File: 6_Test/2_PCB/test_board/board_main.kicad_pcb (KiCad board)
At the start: 4 copper layers, 105.5 x 83 mm, 81 parts, among them J1 PWR_Supply_Pins, J10 Chip_AVSS_GND_Jumpers, J11 Buffer_PWR_Jumper, J12 Reset_PWR_Jumpers, J13 Reset_Signal_Jumpers, J14 1546551-4, J2 Analog_Input_Pins, J3 Digital_Input_Pins, J4 Digital_Output_Pins, J5 Chip_VDD_Jumpers, J6 BNC_Odd, J7 BNC_Even, J8 BNC_Jumpers, J9 Analog_Input_Jumpers, U1 TPS74501PDRVR, U2 ADA4807-1AKSZ-R7, U3 ADA4807-1AKSZ-R7, U4 TPS74501PDRVR, U5 SN74HC74DR, U6 CD4001BM96, U7 SN74LVC245APWR, U8 SN74LVC245APWR

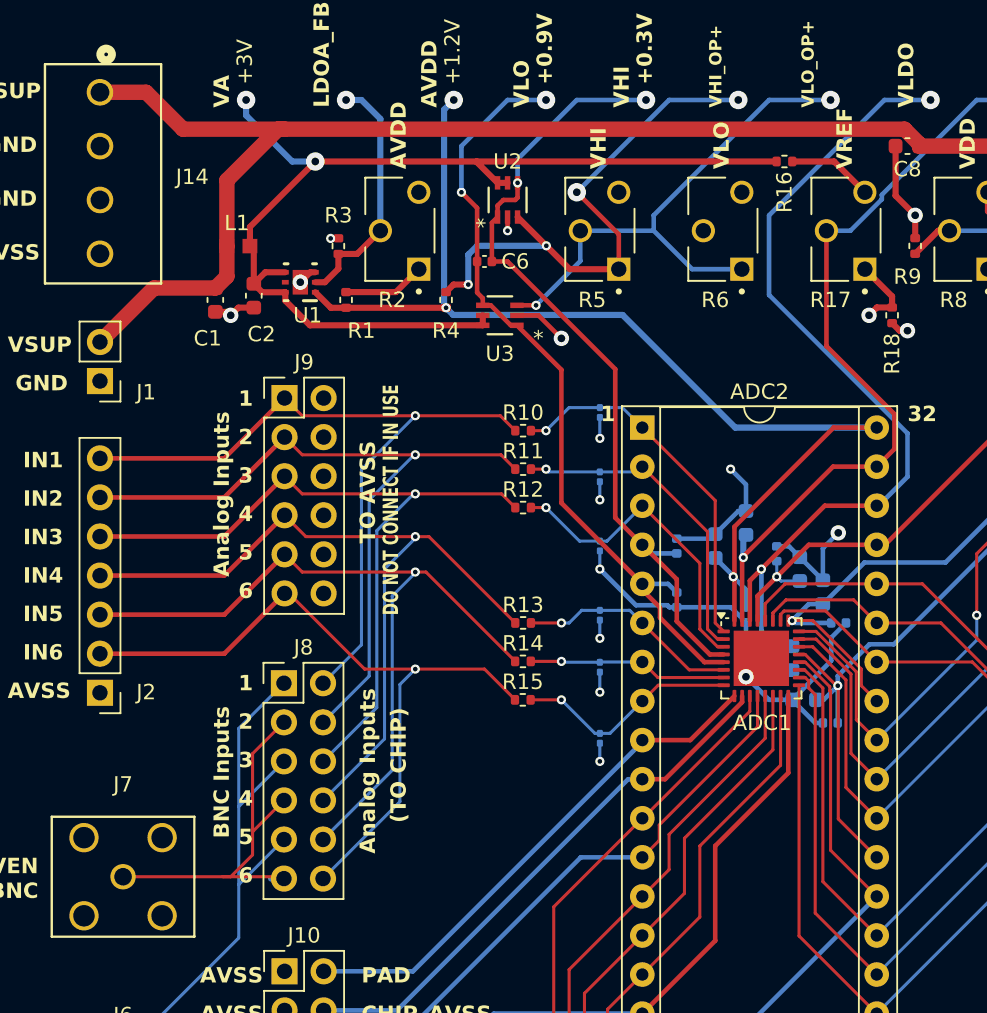
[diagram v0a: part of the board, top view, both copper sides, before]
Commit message: Adjusted potentiometers
Equally spaced potentiometers & added additional silkscreen
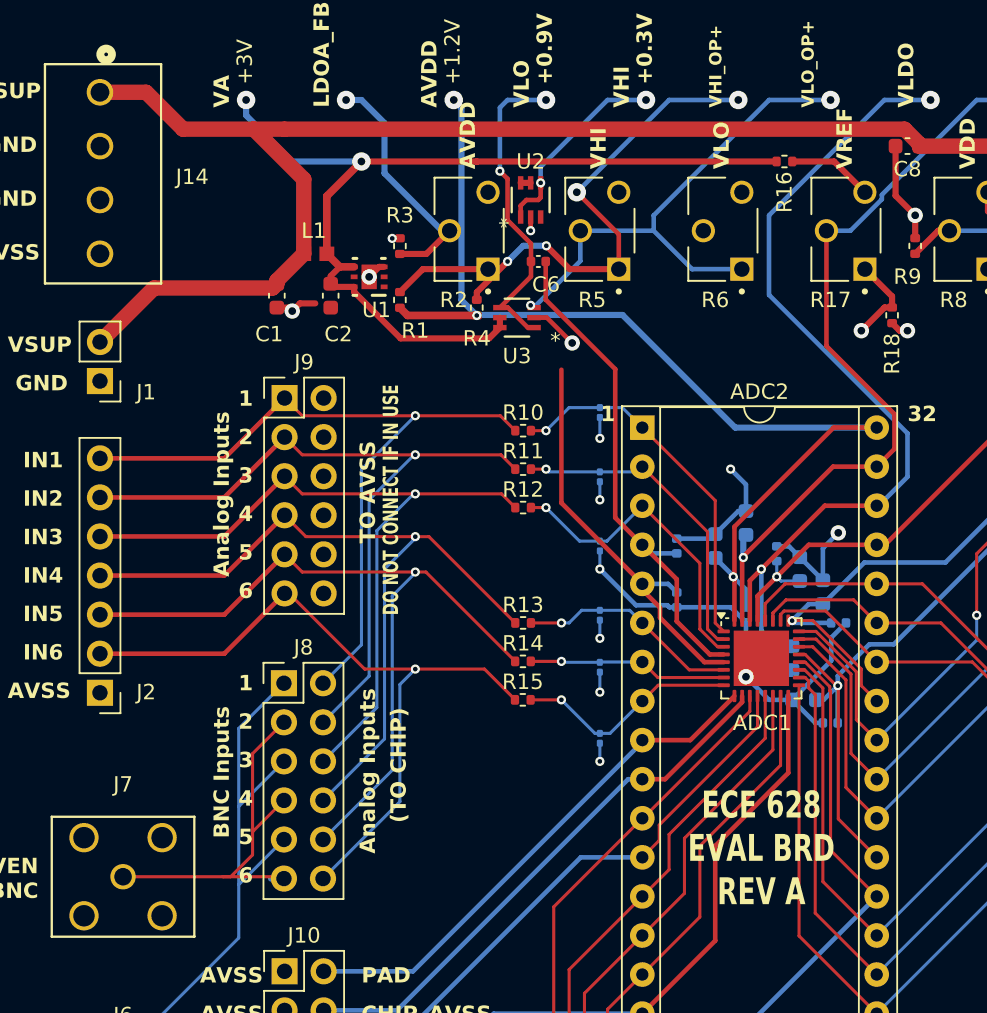
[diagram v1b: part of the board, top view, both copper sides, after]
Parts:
- moved L1 5.02 mm to (93.0, 76.0)
- moved C2 5.00 mm to (94.0, 78.7)
- moved R2 4.50 mm to (103.0, 74.5)
- moved U1 4.49 mm to (96.5, 77.5)
- moved C1 4.01 mm to (90.5, 78.7)
- moved R3 4.00 mm to (98.5, 75.5)
- moved C6 3.50 mm to (107.5, 76.5)
- moved R1 3.50 mm to (98.5, 79.0)
- moved R4 2.06 mm to (103.5, 79.5)
- moved U2 1.50 mm to (107.0, 72.5)
- moved U3 1.12 mm to (106.1, 80.1)
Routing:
- net /AnalogSupply/VA: track 68.5 -> 61.4 mm
- net /ADC/VHI: track 53.1 -> 46.2 mm
- net Net-(U2-+IN): track 36.0 -> 30.7 mm
- net /ADC/AVDD: track 76.0 -> 71.0 mm
- net /ADC/VLO: track 51.1 -> 47.2 mm
- net /AnalogSupply/VSUP: track 98.4 -> 102.2 mm
- net Net-(R1-Pad2): track 5.35 -> 6.35 mm
- net Net-(R17-Pad1): track 4.93 -> 5.85 mm
- net Net-(U3-+IN): track 34.4 -> 33.5 mm
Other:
- board text added: "DN"
- board text added: "ECE 628 EVAL BRD REV A"
- board text added: "UN"

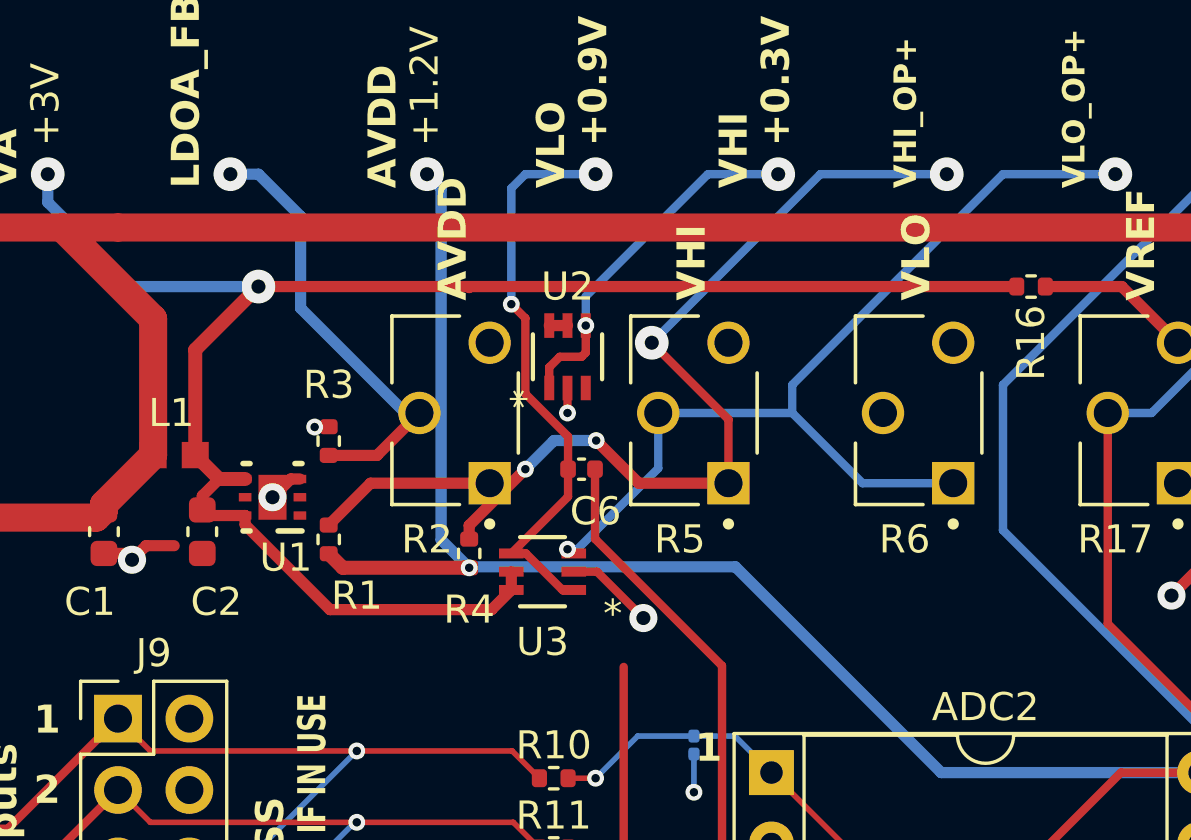
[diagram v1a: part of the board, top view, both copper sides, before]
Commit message: fixed overlapping net issues on final revision
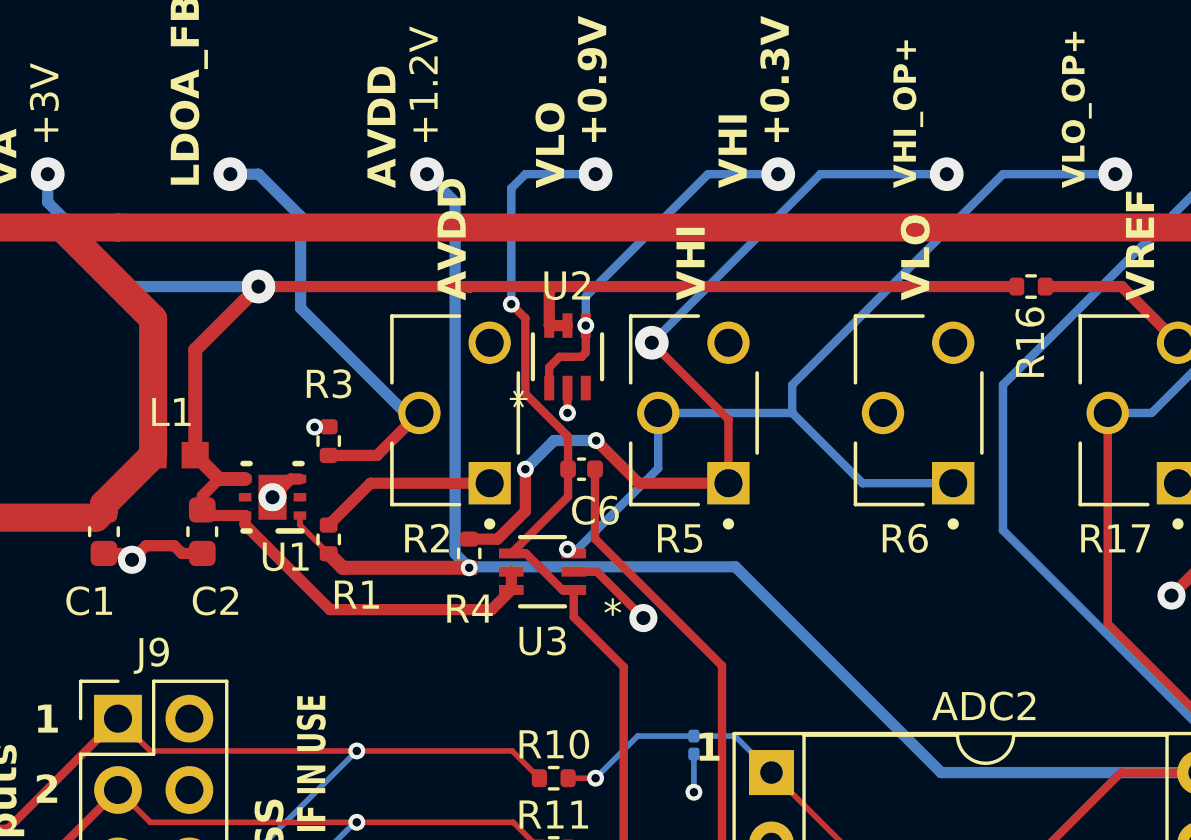
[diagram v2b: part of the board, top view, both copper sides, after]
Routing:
- net /ADC/VLO: track 47.2 -> 50.7 mm
- net /ADC/AVDD: track 71.0 -> 72.8 mm
- net /AnalogSupply/VA: track 61.4 -> 62.9 mm
- net GND: track 117.4 -> 118.5 mm
- net Net-(U2-+IN): track 30.7 -> 31.3 mm
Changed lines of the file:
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@@
 			(outputformat 1)
 			(mirror no)
-			(drillshape 1)
+			(drillshape 0)
 			(scaleselection 1)
 			(outputdirectory "")
@@
 	)
 	(segment
+		(start 109 83.538749)
+		(end 107.2225 81.761249)
+		(width 0.3)
+		(layer "F.Cu")
+		(net 3)
+	)
+	(segment
 		(start 105.519951 79.5)
 		(end 105 79.5)
@@
 	)
 	(segment
+		(start 107.2225 81.761249)
+		(end 107.2225 80.799998)
+		(width 0.3)
+		(layer "F.Cu")
+		(net 3)
+	)
+	(segment
 		(start 105.5 71.127)
 		(end 105.5 73.816002)
@@
 	)
 	(segment
+		(start 97.474999 78.484999)
+		(end 98.5 79.51)
+		(width 0.2)
+		(layer "F.Cu")
+		(net 4)
+	)
+	(segment
 		(start 99 80.01)
 		(end 103.5 80.01)
@@
 	)
 	(segment
+		(start 97.474999 78.150001)
+		(end 97.474999 78.484999)
+		(width 0.2)
+		(layer "F.Cu")
+		(net 4)
+	)
+	(segment
 		(start 98.5 79.51)
 		(end 99 80.01)
@@
 	)
 	(segment
-		(start 102.5 66.5)
+		(start 112.977001 79.977001)
+		(end 120.3 87.3)
+		(width 0.4)
+		(layer "B.Cu")
+		(net 4)
+	)
+	(segment
+		(start 103 67)
 		(end 102 66)
 		(width 0.4)
@@
 	)
 	(segment
-		(start 112.977001 79.977001)
-		(end 120.3 87.3)
+		(start 103 79.51)
+		(end 103 67)
 		(width 0.4)
 		(layer "B.Cu")
@@
 	(segment
 		(start 103.5 80.01)
-		(end 102.5 79.01)
+		(end 103 79.51)
 		(width 0.4)
 		(layer "B.Cu")
@@
 	)
 	(segment
-		(start 102.5 79.01)
-		(end 102.5 66.5)
-		(width 0.4)
-		(layer "B.Cu")
-		(net 4)
-	)
-	(segment
 		(start 103.5 80.01)
 		(end 103.532999 79.977001)
@@
 	)
 	(segment
+		(start 93 79.225)
+		(end 93.275 79.5)
+		(width 0.4)
+		(layer "F.Cu")
+		(net 34)
+	)
+	(segment
 		(start 147.69 130.0362)
 		(end 147.69 131.69)
@@
 	)
 	(segment
+		(start 93.275 79.5)
+		(end 94 79.5)
+		(width 0.4)
+		(layer "F.Cu")
+		(net 34)
+	)
+	(segment
 		(start 142.5856 95.874)
 		(end 143.636598 96.924998)
@@
 	)
 	(segment
-		(start 103.5 70)
-		(end 122.99 70)
+		(start 106.350001 71.38875)
+		(end 106.350001 70.149999)
 		(width 0.4)
 		(layer "F.Cu")
@@
 	)
 	(segment
+		(start 106.5 70)
+		(end 122.99 70)
+		(width 0.4)
+		(layer "F.Cu")
+		(net 35)
+	)
+	(segment
+		(start 106.350001 70.149999)
+		(end 106.5 70)
+		(width 0.4)
+		(layer "F.Cu")
+		(net 35)
+	)
+	(segment
 		(start 98.546001 81.5)
 		(end 104.299998 81.5)
@@
 	)
 	(segment
+		(start 103.5 70)
+		(end 106.5 70)
+		(width 0.4)
+		(layer "F.Cu")
+		(net 35)
+	)
+	(segment
 		(start 94 77.95)
 		(end 94 77.449302)
@@
 	)
 	(segment
-		(start 103.5 78.5)
-		(end 103.5 78.99)
+		(start 105.5 78)
+		(end 104.51 78.99)
 		(width 0.4)
 		(layer "F.Cu")
@@
 	(segment
 		(start 105.5 76.5)
-		(end 103.5 78.5)
+		(end 105.5 78)
 		(width 0.4)
 		(layer "F.Cu")
@@
 		(width 0.4)
 		(layer "F.Cu")
+		(net 48)
+	)
+	(segment
+		(start 104.51 78.99)
+		(end 103.5 78.99)
+		(width 0.4)
+		(layer "F.Cu")

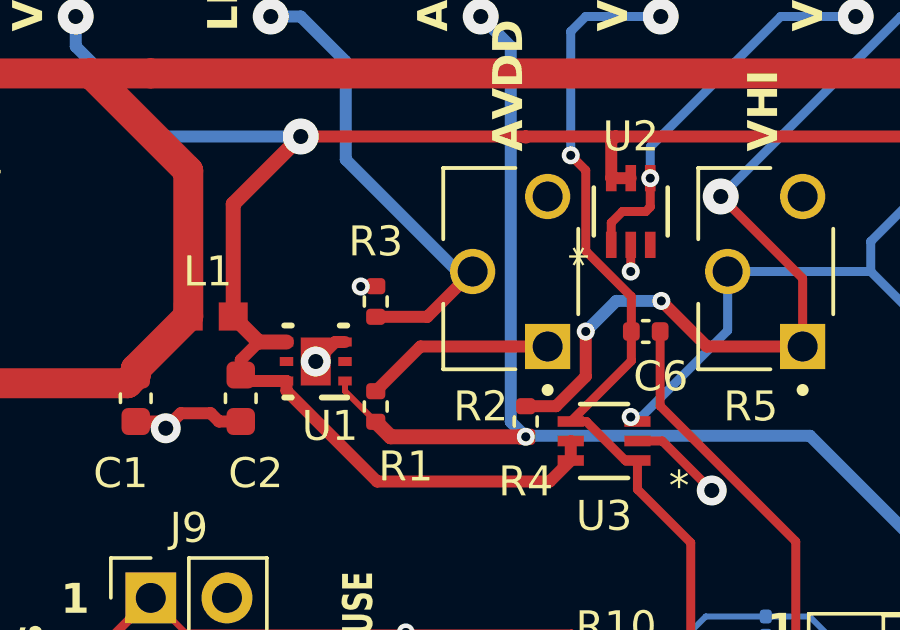
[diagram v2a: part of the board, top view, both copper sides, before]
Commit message: fixed drc errors, refilled zones, generated gerber files
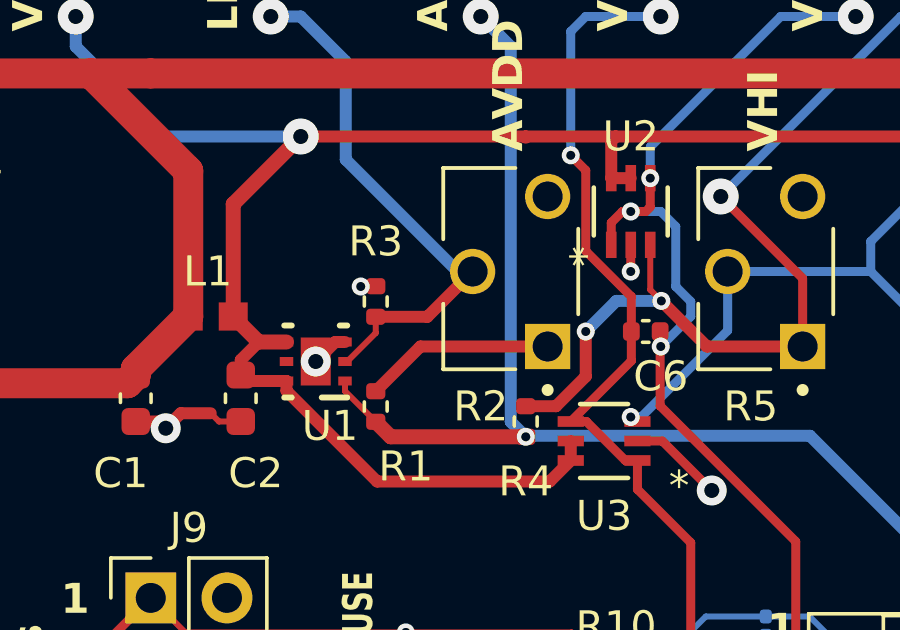
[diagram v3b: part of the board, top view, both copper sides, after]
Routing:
- net /ADC/VHI: track 46.2 -> 52.6 mm, vias 2 -> 4
- net Net-(U2-+IN): track 31.3 -> 33.3 mm
- net Net-(U1-FB): track 16.0 -> 18.0 mm
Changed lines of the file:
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@@
 	)
 	(segment
-		(start 114.26 97.46)
-		(end 114.26 97.85)
+		(start 107.2225 81.761249)
+		(end 107.2225 80.799998)
 		(width 0.3)
 		(layer "F.Cu")
@@
 	)
 	(segment
-		(start 109 83.538749)
-		(end 107.2225 81.761249)
+		(start 114.26 97.46)
+		(end 114.26 97.85)
 		(width 0.3)
 		(layer "F.Cu")
@@
 	)
 	(segment
-		(start 107.02 77.48)
-		(end 105 79.5)
+		(start 109 83.538749)
+		(end 107.2225 81.761249)
 		(width 0.3)
 		(layer "F.Cu")
@@
 	)
 	(segment
-		(start 107.2225 81.761249)
-		(end 107.2225 80.799998)
+		(start 107.02 77.48)
+		(end 105 79.5)
 		(width 0.3)
 		(layer "F.Cu")
@@
 	)
 	(segment
+		(start 97.474999 78.150001)
+		(end 97.474999 78.484999)
+		(width 0.2)
+		(layer "F.Cu")
+		(net 4)
+	)
+	(segment
 		(start 120.25 99.85)
 		(end 120.25 93.75)
@@
 	)
 	(segment
-		(start 97.474999 78.484999)
-		(end 98.5 79.51)
-		(width 0.2)
-		(layer "F.Cu")
-		(net 4)
-	)
-	(segment
 		(start 99 80.01)
 		(end 103.5 80.01)
@@
 	)
 	(segment
-		(start 97.474999 78.150001)
-		(end 97.474999 78.484999)
-		(width 0.2)
+		(start 98.5 79.51)
+		(end 99 80.01)
+		(width 0.5)
 		(layer "F.Cu")
 		(net 4)
 	)
 	(segment
-		(start 98.5 79.51)
-		(end 99 80.01)
-		(width 0.5)
+		(start 97.474999 78.484999)
+		(end 98.5 79.51)
+		(width 0.2)
 		(layer "F.Cu")
 		(net 4)
@@
 	)
 	(segment
-		(start 103 67)
-		(end 102 66)
-		(width 0.4)
-		(layer "B.Cu")
-		(net 4)
-	)
-	(segment
-		(start 103 79.51)
-		(end 103 67)
-		(width 0.4)
-		(layer "B.Cu")
-		(net 4)
-	)
-	(segment
-		(start 103.5 80.01)
-		(end 103 79.51)
-		(width 0.4)
-		(layer "B.Cu")
-		(net 4)
-	)
-	(segment
 		(start 121 97.827)
 		(end 120.173 97)
@@
 	)
 	(segment
+		(start 103 79.51)
+		(end 103 67)
+		(width 0.4)
+		(layer "B.Cu")
+		(net 4)
+	)
+	(segment
+		(start 103.5 80.01)
+		(end 103 79.51)
+		(width 0.4)
+		(layer "B.Cu")
+		(net 4)
+	)
+	(segment
 		(start 103.5 80.01)
 		(end 103.532999 79.977001)
@@
 	)
 	(segment
+		(start 103 67)
+		(end 102 66)
+		(width 0.4)
+		(layer "B.Cu")
+		(net 4)
+	)
+	(segment
 		(start 119.55 104.05)
 		(end 115.29 104.05)
@@
 	)
 	(segment
+		(start 107 72.5)
+		(end 107.5 72.5)
+		(width 0.3)
+		(layer "F.Cu")
+		(net 7)
+	)
+	(segment
 		(start 107.5 72.5)
 		(end 107.649999 72.350001)
@@
 	(segment
 		(start 106.723101 72.5)
-		(end 107.5 72.5)
+		(end 107 72.5)
 		(width 0.3)
 		(layer "F.Cu")
@@
 	)
 	(via
+		(at 108 77)
+		(size 0.6)
+		(drill 0.3)
+		(layers "F.Cu" "B.Cu")
+		(net 7)
+	)
+	(via
+		(at 107 72.5)
+		(size 0.6)
+		(drill 0.3)
+		(layers "F.Cu" "B.Cu")
+		(net 7)
+	)
+	(via
 		(at 114.5 66)
 		(size 1.2)
@@
 	)
 	(segment
+		(start 108.5 73)
+		(end 108.5 75)
+		(width 0.3)
+		(layer "B.Cu")
+		(net 7)
+	)
+	(segment
 		(start 116.5 95.48)
 		(end 114.82 95.48)
@@
 	)
 	(segment
+		(start 109 75.5)
+		(end 109 76)
+		(width 0.3)
+		(layer "B.Cu")
+		(net 7)
+	)
+	(segment
+		(start 108.5 75)
+		(end 109 75.5)
+		(width 0.3)
+		(layer "B.Cu")
+		(net 7)
+	)
+	(segment
+		(start 107 72.5)
+		(end 108 72.5)
+		(width 0.3)
+		(layer "B.Cu")
+		(net 7)
+	)
+	(segment
 		(start 107.649999 70.350001)
 		(end 107.649999 71.38875)
@@
 	)
 	(segment
+		(start 108 72.5)
+		(end 108.5 73)
+		(width 0.3)
+		(layer "B.Cu")
+		(net 7)
+	)
+	(segment
+		(start 109 76)
+		(end 108 77)
+		(width 0.3)
+		(layer "B.Cu")
+		(net 7)
+	)
+	(segment
 		(start 114.5 66)
 		(end 112 66)
@@
 	)
 	(segment
+		(start 93.275 79.5)
+		(end 93 79.225)
+		(width 0.2)
+		(layer "F.Cu")
+		(net 34)
+	)
+	(segment
 		(start 151.5 132.5)
 		(end 150.23 131.23)
@@
 	)
 	(segment
-		(start 93 79.225)
-		(end 93.275 79.5)
-		(width 0.4)
-		(layer "F.Cu")
-		(net 34)
-	)
-	(segment
 		(start 147.69 130.0362)
 		(end 147.69 131.69)
@@
 	)
 	(segment
-		(start 93.275 79.5)
-		(end 94 79.5)
-		(width 0.4)
-		(layer "F.Cu")
-		(net 34)
-	)
-	(segment
 		(start 142.5856 95.874)
 		(end 143.636598 96.924998)
@@
 	)
 	(segment
+		(start 94 79.5)
+		(end 93.275 79.5)
+		(width 0.2)
+		(layer "F.Cu")
+		(net 34)
+	)
+	(segment
 		(start 151.5 132.5)
 		(end 152.2874 132.5)
@@
 	)
 	(segment
-		(start 106.5 70)
-		(end 122.99 70)
+		(start 103.5 70)
+		(end 106.5 70)
 		(width 0.4)
 		(layer "F.Cu")
@@
 	)
 	(segment
+		(start 106.5 70)
+		(end 122.99 70)
+		(width 0.4)
+		(layer "F.Cu")
+		(net 35)
+	)
+	(segment
 		(start 98.546001 81.5)
 		(end 104.299998 81.5)
@@
 	)
 	(segment
-		(start 103.5 70)
-		(end 106.5 70)
-		(width 0.4)
-		(layer "F.Cu")
-		(net 35)
-	)
-	(segment
 		(start 94 77.95)
 		(end 94 77.449302)
@@
 	)
 	(segment
+		(start 98.5 76.549999)
+		(end 98.5 76.01)
+		(width 0.2)
+		(layer "F.Cu")
+		(net 47)
+	)
+	(segment
+		(start 97.549999 77.5)
+		(end 98.5 76.549999)
+		(width 0.2)
+		(layer "F.Cu")
+		(net 47)
+	)
+	(segment
+		(start 97.474999 77.5)
+		(end 97.549999 77.5)
+		(width 0.2)
+		(layer "F.Cu")
+		(net 47)
+	)
+	(segment
 		(start 100.22 76.01)
 		(end 101.73 74.5)
@@
 	)
 	(segment
-		(start 105.5 78)
-		(end 104.51 78.99)
-		(width 0.4)
-		(layer "F.Cu")
-		(net 48)
-	)
-	(segment
-		(start 105.5 76.5)
-		(end 105.5 78)
-		(width 0.4)
+		(start 107.649999 75.111249)
+		(end 108.019375 75.480625)
+		(width 0.2)
 		(layer "F.Cu")
 		(net 48)
@@
 	)
 	(segment
+		(start 105.5 78)
+		(end 104.51 78.99)
+		(width 0.4)
+		(layer "F.Cu")
+		(net 48)
+	)
+	(segment
 		(start 109.538749 77)
 		(end 108.019375 75.480625)
@@
 	)
 	(segment
+		(start 105.5 76.5)
+		(end 105.5 78)
+		(width 0.4)
+		(layer "F.Cu")
+		(net 48)
+	)
+	(segment
 		(start 112.73 74.73)
 		(end 110 72)
@@
 		(layer "F.Cu")
 		(net 48)
+	)
+	(segment
+		(start 107.649999 73.61125)
+		(end 107.649999 75.111249)
+		(width 0.2)
+		(layer "F.Cu")
+		(net 48)
